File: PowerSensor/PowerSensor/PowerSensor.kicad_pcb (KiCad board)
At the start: 2 copper layers, 40.8 x 26.4 mm, 11 parts, among them J1 Screw_Terminal_01x02, J2 Screw_Terminal_01x05, J3 Screw_Terminal_01x02, J4 Screw_Terminal_01x02, U1 ACS712ELCTR-20A-T_NRND

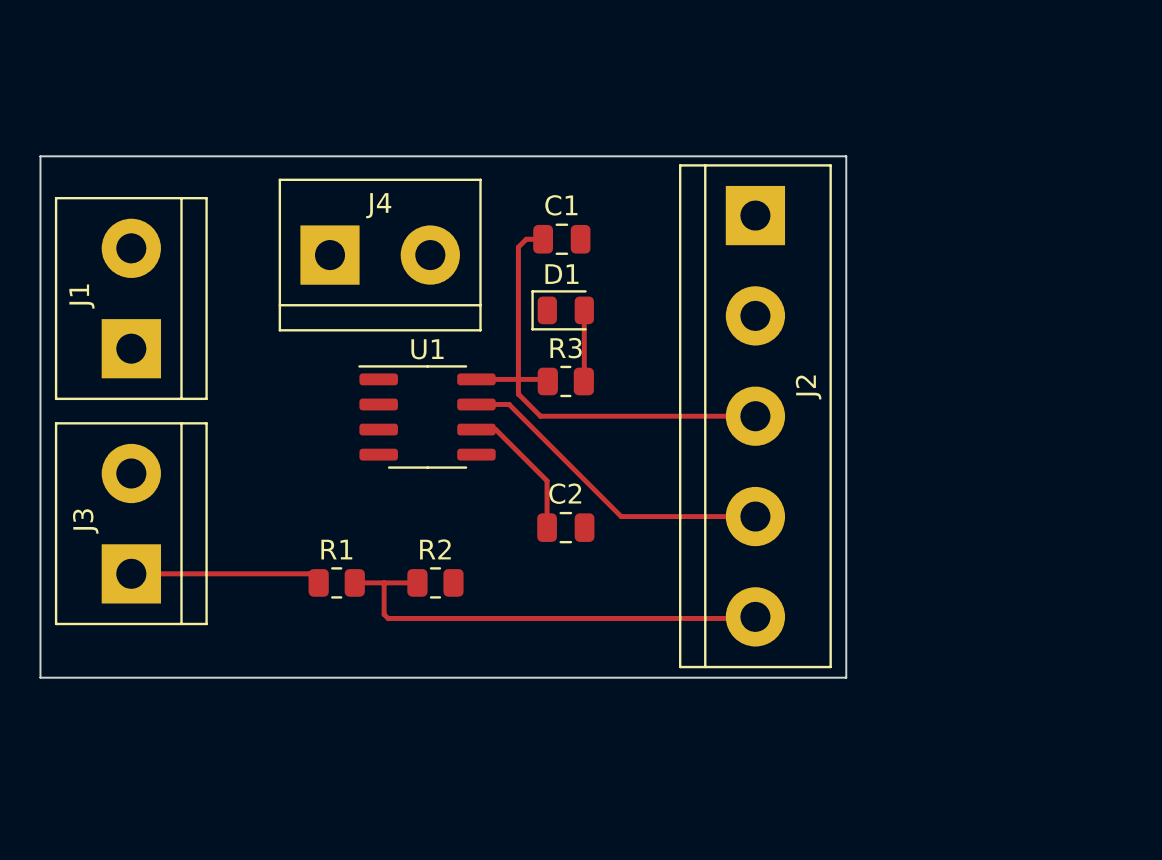
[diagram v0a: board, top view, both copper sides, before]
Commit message: Change the main project with another project saved on desktop
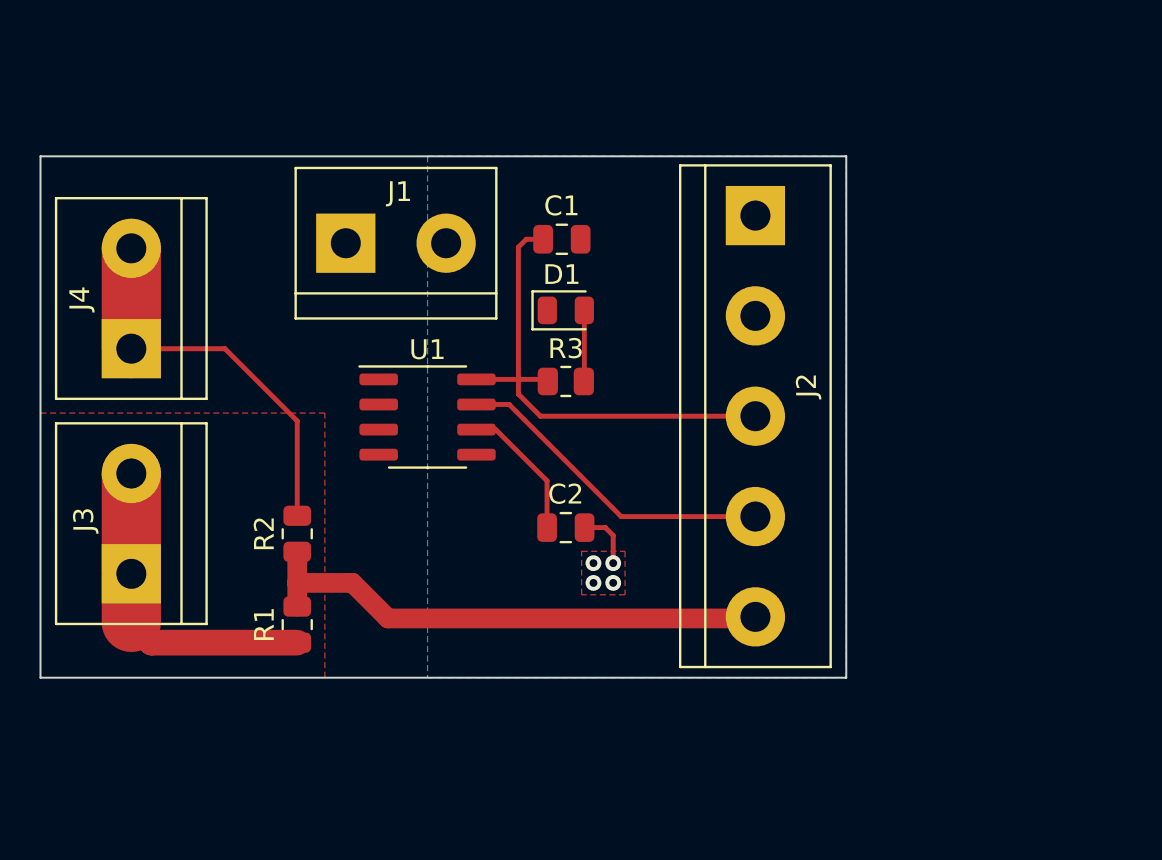
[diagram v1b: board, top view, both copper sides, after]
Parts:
- moved J1 12.1 mm to (87.9, 74.6), turned to 0 degrees
- moved J4 11.1 mm to (77.0, 79.9), turned to 90 degrees
- moved R2 7.43 mm to (85.4, 89.3), turned to 90 degrees
- moved R1 2.91 mm to (85.4, 93.9), turned to 90 degrees
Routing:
- net Battery(-): track 0.00 -> 19.8 mm
- net Battery(+): track 9.68 -> 16.4 mm
- net Vsens: track 23.7 -> 26.8 mm
- net GND: track 0.00 -> 3.02 mm, vias 0 -> 4
- added copper zone on F.Cu, net Battery(+)
- added copper zone on B.Cu, net GND
- added copper zone on F.Cu, net GND

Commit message: Add Decoupling Cap 1uF to 5V
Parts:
- added C3: 1uF, Capacitor_SMD:C_0805_2012Metric, F.Cu at (95.0, 89.2)
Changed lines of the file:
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@@
+    )
+  )
+  (footprint "Capacitor_SMD:C_0805_2012Metric" (layer "F.Cu")
+    (at 95.05 89.2)
+    (descr "Capacitor SMD 0805 (2012 Metric), square (rectangular) end terminal, IPC_7351 nominal, (Body size source: IPC-SM-782 page 76, https://www.pcb-3d.com/wordpress/wp-content/uploads/ipc-sm-782a_amendment_1_and_2.pdf, https://docs.google.com/spreadsheets/d/1BsfQQcO9C6DZCsRaXUlFlo91Tg2WpOkGARC1WS5S8t0/edit?usp=sharing), generated with kicad-footprint-generator")
+    (tags "capacitor")
+    (property "Sheetfile" "PowerSensor.kicad_sch")
+    (property "Sheetname" "")
+    (property "ki_description" "Unpolarized capacitor")
+    (property "ki_keywords" "cap capacitor")
+    (attr smd)
+    (fp_text reference "C3" (at 0 -1.68) (layer "F.SilkS")
+        (effects (font (size 1 1) (thickness 0.15)))
+    )
+    (fp_text value "1uF" (at 0 1.68) (layer "F.Fab")
+        (effects (font (size 1 1) (thickness 0.15)))
+    )
+    (fp_text user "${REFERENCE}" (at 0 0) (layer "F.Fab")
+        (effects (font (size 0.5 0.5) (thickness 0.08)))
+    )
+    (fp_line (start -0.261252 -0.735) (end 0.261252 -0.735)
+      (stroke (width 0.12) (type solid)) (layer "F.SilkS"))
+    (fp_line (start -0.261252 0.735) (end 0.261252 0.735)
+      (stroke (width 0.12) (type solid)) (layer "F.SilkS"))
+    (fp_line (start -1.7 -0.98) (end 1.7 -0.98)
+      (stroke (width 0.05) (type solid)) (layer "F.CrtYd"))
+    (fp_line (start -1.7 0.98) (end -1.7 -0.98)
+      (stroke (width 0.05) (type solid)) (layer "F.CrtYd"))
+    (fp_line (start 1.7 -0.98) (end 1.7 0.98)
+      (stroke (width 0.05) (type solid)) (layer "F.CrtYd"))
+    (fp_line (start 1.7 0.98) (end -1.7 0.98)
+      (stroke (width 0.05) (type solid)) (layer "F.CrtYd"))
+    (fp_line (start -1 -0.625) (end 1 -0.625)
+      (stroke (width 0.1) (type solid)) (layer "F.Fab"))
+    (fp_line (start -1 0.625) (end -1 -0.625)
+      (stroke (width 0.1) (type solid)) (layer "F.Fab"))
+    (fp_line (start 1 -0.625) (end 1 0.625)
+      (stroke (width 0.1) (type solid)) (layer "F.Fab"))
+    (fp_line (start 1 0.625) (end -1 0.625)
+      (stroke (width 0.1) (type solid)) (layer "F.Fab"))
+    (pad "1" smd roundrect (at -0.95 0) (size 1 1.45) (layers "F.Cu" "F.Paste" "F.Mask") (roundrect_rratio 0.25)
+      (net 6 "+5V") (pintype "passive"))
+    (pad "2" smd roundrect (at 0.95 0) (size 1 1.45) (layers "F.Cu" "F.Paste" "F.Mask") (roundrect_rratio 0.25)
+      (net 1 "GND") (pintype "passive"))
+    (model "${KICAD6_3DMODEL_DIR}/Capacitor_SMD.3dshapes/C_0805_2012Metric.wrl"
+      (offset (xyz 0 0 0))
+      (scale (xyz 1 1 1))
+      (rotate (xyz 0 0 0))
     )
   )

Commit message: Add decupling Cap to 5V
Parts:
- added C4: 1uF, Capacitor_SMD:C_0805_2012Metric, F.Cu at (96.0, 67.0)
- moved C3 17.8 mm to (98.8, 71.8)
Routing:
- net +5V: track 25.0 -> 29.1 mm
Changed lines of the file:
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@@
     (property "ki_keywords" "cap capacitor")
     (attr smd)
-    (fp_text reference "C1" (at 0 -1.68) (layer "F.SilkS")
+    (fp_text reference "C1" (at 2.8 0) (layer "F.SilkS")
         (effects (font (size 1 1) (thickness 0.15)))
     )
@@
   )
   (footprint "Capacitor_SMD:C_0805_2012Metric" (layer "F.Cu")
-    (at 95.05 89.2)
+    (at 95.95 67)
     (descr "Capacitor SMD 0805 (2012 Metric), square (rectangular) end terminal, IPC_7351 nominal, (Body size source: IPC-SM-782 page 76, https://www.pcb-3d.com/wordpress/wp-content/uploads/ipc-sm-782a_amendment_1_and_2.pdf, https://docs.google.com/spreadsheets/d/1BsfQQcO9C6DZCsRaXUlFlo91Tg2WpOkGARC1WS5S8t0/edit?usp=sharing), generated with kicad-footprint-generator")
     (tags "capacitor")
@@
     (property "ki_keywords" "cap capacitor")
     (attr smd)
-    (fp_text reference "C3" (at 0 -1.68) (layer "F.SilkS")
+    (fp_text reference "C4" (at 0 -1.68) (layer "F.SilkS")
+        (effects (font (size 1 1) (thickness 0.15)))
+    )
+    (fp_text value "1uF" (at 0 1.68) (layer "F.Fab")
+        (effects (font (size 1 1) (thickness 0.15)))
+    )
+    (fp_text user "${REFERENCE}" (at 0 0) (layer "F.Fab")
+        (effects (font (size 0.5 0.5) (thickness 0.08)))
+    )
+    (fp_line (start -0.261252 -0.735) (end 0.261252 -0.735)
+      (stroke (width 0.12) (type solid)) (layer "F.SilkS"))
+    (fp_line (start -0.261252 0.735) (end 0.261252 0.735)
+      (stroke (width 0.12) (type solid)) (layer "F.SilkS"))
+    (fp_line (start -1.7 -0.98) (end 1.7 -0.98)
+      (stroke (width 0.05) (type solid)) (layer "F.CrtYd"))
+    (fp_line (start -1.7 0.98) (end -1.7 -0.98)
+      (stroke (width 0.05) (type solid)) (layer "F.CrtYd"))
+    (fp_line (start 1.7 -0.98) (end 1.7 0.98)
+      (stroke (width 0.05) (type solid)) (layer "F.CrtYd"))
+    (fp_line (start 1.7 0.98) (end -1.7 0.98)
+      (stroke (width 0.05) (type solid)) (layer "F.CrtYd"))
+    (fp_line (start -1 -0.625) (end 1 -0.625)
+      (stroke (width 0.1) (type solid)) (layer "F.Fab"))
+    (fp_line (start -1 0.625) (end -1 -0.625)
+      (stroke (width 0.1) (type solid)) (layer "F.Fab"))
+    (fp_line (start 1 -0.625) (end 1 0.625)
+      (stroke (width 0.1) (type solid)) (layer "F.Fab"))
+    (fp_line (start 1 0.625) (end -1 0.625)
+      (stroke (width 0.1) (type solid)) (layer "F.Fab"))
+    (pad "1" smd roundrect (at -0.95 0) (size 1 1.45) (layers "F.Cu" "F.Paste" "F.Mask") (roundrect_rratio 0.25)
+      (net 6 "+5V") (pintype "passive"))
+    (pad "2" smd roundrect (at 0.95 0) (size 1 1.45) (layers "F.Cu" "F.Paste" "F.Mask") (roundrect_rratio 0.25)
+      (net 1 "GND") (pintype "passive"))
+    (model "${KICAD6_3DMODEL_DIR}/Capacitor_SMD.3dshapes/C_0805_2012Metric.wrl"
+      (offset (xyz 0 0 0))
+      (scale (xyz 1 1 1))
+      (rotate (xyz 0 0 0))
+    )
+  )
+  (footprint "Capacitor_SMD:C_0805_2012Metric" (layer "F.Cu")
+    (at 98.75 71.8)
+    (descr "Capacitor SMD 0805 (2012 Metric), square (rectangular) end terminal, IPC_7351 nominal, (Body size source: IPC-SM-782 page 76, https://www.pcb-3d.com/wordpress/wp-content/uploads/ipc-sm-782a_amendment_1_and_2.pdf, https://docs.google.com/spreadsheets/d/1BsfQQcO9C6DZCsRaXUlFlo91Tg2WpOkGARC1WS5S8t0/edit?usp=sharing), generated with kicad-footprint-generator")
+    (tags "capacitor")
+    (property "Sheetfile" "PowerSensor.kicad_sch")
+    (property "Sheetname" "")
+    (property "ki_description" "Unpolarized capacitor")
+    (property "ki_keywords" "cap capacitor")
+    (attr smd)
+    (fp_text reference "C3" (at 2.85 0) (layer "F.SilkS")
         (effects (font (size 1 1) (thickness 0.15)))
     )
@@
   (segment (start 77 74.86) (end 77 79.94) (width 3) (layer "F.Cu") (net 5))
   (segment (start 77 79.94) (end 81.74 79.94) (width 0.25) (layer "F.Cu") (net 5))
+  (segment (start 96.8 71.8) (end 96.6 72) (width 0.25) (layer "F.Cu") (net 6))
   (segment (start 97.85 74.4) (end 97 74.4) (width 0.25) (layer "F.Cu") (net 6))
   (segment (start 96.6 81.495) (end 97.9825 81.495) (width 0.25) (layer "F.Cu") (net 6))
@@
   (segment (start 97.72 83.36) (end 96.6 82.24) (width 0.25) (layer "F.Cu") (net 6))
   (segment (start 96.6 82.24) (end 96.6 81.495) (width 0.25) (layer "F.Cu") (net 6))
+  (segment (start 96.6 72) (end 96.6 74.8) (width 0.25) (layer "F.Cu") (net 6))
+  (segment (start 97.8 71.8) (end 96.8 71.8) (width 0.25) (layer "F.Cu") (net 6))
   (segment (start 97 74.4) (end 96.6 74.8) (width 0.25) (layer "F.Cu") (net 6))
   (segment (start 94.475 82.765) (end 96.128604 82.765) (width 0.25) (layer "F.Cu") (net 7))

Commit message: Re desgin PCB
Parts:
- removed C4: 1uF, Capacitor_SMD:C_0805_2012Metric
- removed J2: Screw_Terminal_01x05, TerminalBlock:TerminalBlock_bornier-5_P5.08mm
- added J5: Screw_Terminal_01x04, TerminalBlock:TerminalBlock_bornier-4_P5.08mm, F.Cu at (118.8, 84.4)
- J1: value Screw_Terminal_01x02 -> Current Sens
- J3: value Screw_Terminal_01x02 -> BAT+
- J4: value Screw_Terminal_01x02 -> BAT-
- moved J1 34.4 mm to (111.7, 99.4), turned to 180 degrees
- moved J4 27.6 mm to (95.8, 100.1)
- moved R2 20.4 mm to (102.0, 101.2), turned to -90 degrees
- moved C3 20.1 mm to (112.2, 86.8), turned to 90 degrees
- moved U1 19.3 mm to (109.2, 92.2)
- moved J3 18.9 mm to (95.8, 89.5)
- moved R1 17.0 mm to (102.0, 97.4), turned to -90 degrees
- moved C1 16.5 mm to (109.8, 86.8), turned to 90 degrees
- moved D1 10.7 mm to (105.2, 86.7), turned to 90 degrees
- moved R3 9.83 mm to (107.4, 86.7), turned to 90 degrees
- moved C2 4.42 mm to (102.8, 86.8), turned to 90 degrees
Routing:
- net IN+: track 0.00 -> 14.8 mm
- net +5V: track 29.1 -> 16.4 mm
- net IN-: track 0.00 -> 8.64 mm
- net VIOUT: track 16.5 -> 8.35 mm
- net Battery(-): track 19.8 -> 12.1 mm
- net Net-(U1-FILTER): track 7.02 -> 13.4 mm
- net Vsens: track 26.8 -> 20.9 mm
- net GND: track 3.02 -> 0.00 mm, vias 4 -> 0
- net Battery(+): track 16.4 -> 14.7 mm
- net Net-(D1-A): track 3.61 -> 2.20 mm
- removed copper zone on F.Cu, net Battery(+)
- removed copper zone on F.Cu, net GND
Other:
- board size 40.8 x 26.4 mm -> 35.6 x 22.6 mm
- board text added: "+5V"
- board text added: "GND"
- board text added: "ISens"
- board text added: "VSens"

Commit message: optimization for PCB
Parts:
- turned D1 to -90 degrees
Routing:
- net GND: track 0.00 -> 25.8 mm, vias 0 -> 3
- net Net-(D1-A): track 2.20 -> 3.14 mm
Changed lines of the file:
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@@
   )
   (footprint "LED_SMD:LED_0805_2012Metric" (layer "F.Cu")
-    (at 105.2 86.7375 90)
+    (at 105.2 86.7375 -90)
     (descr "LED SMD 0805 (2012 Metric), square (rectangular) end terminal, IPC_7351 nominal, (Body size source: https://docs.google.com/spreadsheets/d/1BsfQQcO9C6DZCsRaXUlFlo91Tg2WpOkGARC1WS5S8t0/edit?usp=sharing), generated with kicad-footprint-generator")
     (tags "LED")
@@
     (fp_line (start 1 0.6) (end 1 -0.6)
       (stroke (width 0.1) (type solid)) (layer "F.Fab"))
-    (pad "1" smd roundrect (at -0.9375 0 90) (size 0.975 1.4) (layers "F.Cu" "F.Paste" "F.Mask") (roundrect_rratio 0.25)
+    (pad "1" smd roundrect (at -0.9375 0 270) (size 0.975 1.4) (layers "F.Cu" "F.Paste" "F.Mask") (roundrect_rratio 0.25)
       (net 1 "GND") (pinfunction "K") (pintype "passive"))
-    (pad "2" smd roundrect (at 0.9375 0 90) (size 0.975 1.4) (layers "F.Cu" "F.Paste" "F.Mask") (roundrect_rratio 0.25)
+    (pad "2" smd roundrect (at 0.9375 0 270) (size 0.975 1.4) (layers "F.Cu" "F.Paste" "F.Mask") (roundrect_rratio 0.25)
       (net 2 "Net-(D1-A)") (pinfunction "A") (pintype "passive"))
     (model "${KICAD6_3DMODEL_DIR}/LED_SMD.3dshapes/LED_0805_2012Metric.wrl"
@@
   (gr_rect (start 91.4 81.2) (end 127 103.8)
     (stroke (width 0.1) (type default)) (fill none) (layer "Edge.Cuts"))
-  (gr_text "GND" (at 123.4 84.8) (layer "F.SilkS")
+  (gr_text "ISens" (at 123 94.8) (layer "F.SilkS")
+    (effects (font (size 0.75 0.75) (thickness 0.15)) (justify left bottom))
+  )
+  (gr_text "GND" (at 123.2 84.8) (layer "F.SilkS")
     (effects (font (size 1 1) (thickness 0.15)) (justify left bottom))
   )
-  (gr_text "ISens" (at 123 94.8) (layer "Edge.Cuts")
+  (gr_text "+5V" (at 123 90) (layer "F.SilkS")
+    (effects (font (size 1 1) (thickness 0.15)) (justify left bottom))
+  )
+  (gr_text "VSens" (at 123 99.8) (layer "F.SilkS")
     (effects (font (size 0.75 0.75) (thickness 0.15)) (justify left bottom))
   )
-  (gr_text "+5V" (at 123.4 90) (layer "Edge.Cuts")
-    (effects (font (size 1 1) (thickness 0.15)) (justify left bottom))
-  )
-  (gr_text "VSens" (at 123 99.8) (layer "Edge.Cuts")
-    (effects (font (size 0.75 0.75) (thickness 0.15)) (justify left bottom))
-  )
-  (segment (start 107.4 85.8) (end 105.2 85.8) (width 0.25) (layer "F.Cu") (net 2))
+  (segment (start 111.675 94.105) (end 113.295 94.105) (width 0.25) (layer "F.Cu") (net 1))
+  (segment (start 113.295 94.105) (end 113.6 93.8) (width 0.25) (layer "F.Cu") (net 1))
+  (segment (start 109.8 84.36) (end 105.2 84.36) (width 0.25) (layer "F.Cu") (net 1))
+  (segment (start 112.2 84.36) (end 109.8 84.36) (width 0.25) (layer "F.Cu") (net 1))
+  (segment (start 102.84 84.36) (end 102.8 84.4) (width 0.25) (layer "F.Cu") (net 1))
+  (segment (start 112.2 85.8) (end 112.2 84.36) (width 0.25) (layer "F.Cu") (net 1))
+  (segment (start 109.8 85.8) (end 109.8 84.36) (width 0.25) (layer "F.Cu") (net 1))
+  (segment (start 105.2 85.8) (end 105.2 84.36) (width 0.25) (layer "F.Cu") (net 1))
+  (segment (start 118.8 84.36) (end 112.2 84.36) (width 0.25) (layer "F.Cu") (net 1))
+  (segment (start 102.8 84.4) (end 102.8 85.8) (width 0.25) (layer "F.Cu") (net 1))
+  (segment (start 113.6 92.8) (end 113.6 94.8) (width 0.25) (layer "F.Cu") (net 1))
+  (segment (start 105.2 84.36) (end 102.84 84.36) (width 0.25) (layer "F.Cu") (net 1))
+  (via (at 113.6 93.8) (size 0.8) (drill 0.4) (layers "F.Cu" "B.Cu") (free) (net 1))
+  (via (at 113.6 94.8) (size 0.8) (drill 0.4) (layers "F.Cu" "B.Cu") (free) (net 1))
+  (via (at 113.6 92.8) (size 0.8) (drill 0.4) (layers "F.Cu" "B.Cu") (free) (net 1))
+  (segment (start 107.4 85.8) (end 106.8 85.8) (width 0.25) (layer "F.Cu") (net 2))
+  (segment (start 105.2 87.4) (end 105.2 87.675) (width 0.25) (layer "F.Cu") (net 2))
+  (segment (start 106.8 85.8) (end 105.2 87.4) (width 0.25) (layer "F.Cu") (net 2))
   (segment (start 111.74 99.12) (end 106.725 94.105) (width 0.2) (layer "F.Cu") (net 3))
   (segment (start 111.74 99.4) (end 111.74 99.12) (width 0.2) (layer "F.Cu") (net 3))
@@
     (polygon
       (pts
-        (xy 127 81.2)
-        (xy 91.4 81.2)
-        (xy 91.4 103.8)
-        (xy 127 103.8)
+        (xy 122.8 81.2)
+        (xy 122.8 103.8)
+        (xy 101 103.8)
+        (xy 101 81.2)
       )
     )
